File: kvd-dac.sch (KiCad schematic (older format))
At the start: 76 parts, among them J1 CONN_01X03, U1 ADG1412, U10 74HC595, U11 OPA2189, U12 MUX507, U13 AD8428, U14 AD8428, U15 AD8428, U16 AD8428, U17 OPA2189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

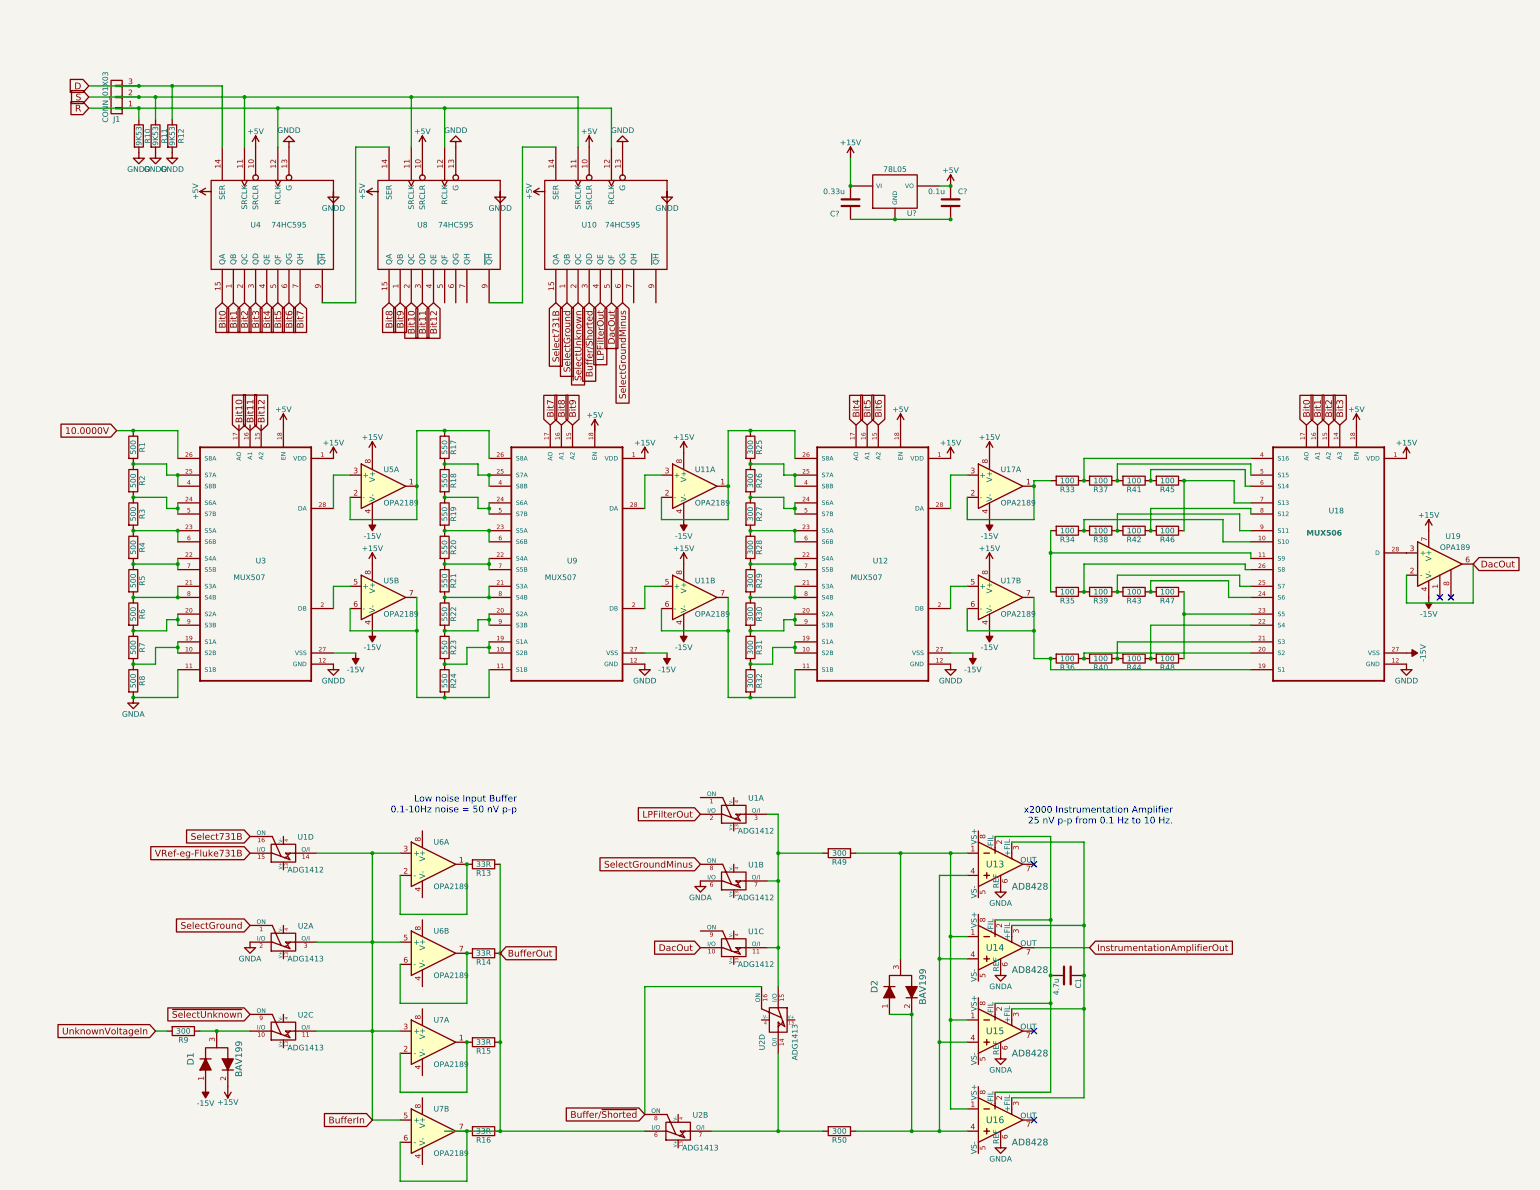
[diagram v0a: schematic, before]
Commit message: Add files via upload
Updated opamps to ada4522 because they have lower bias current.
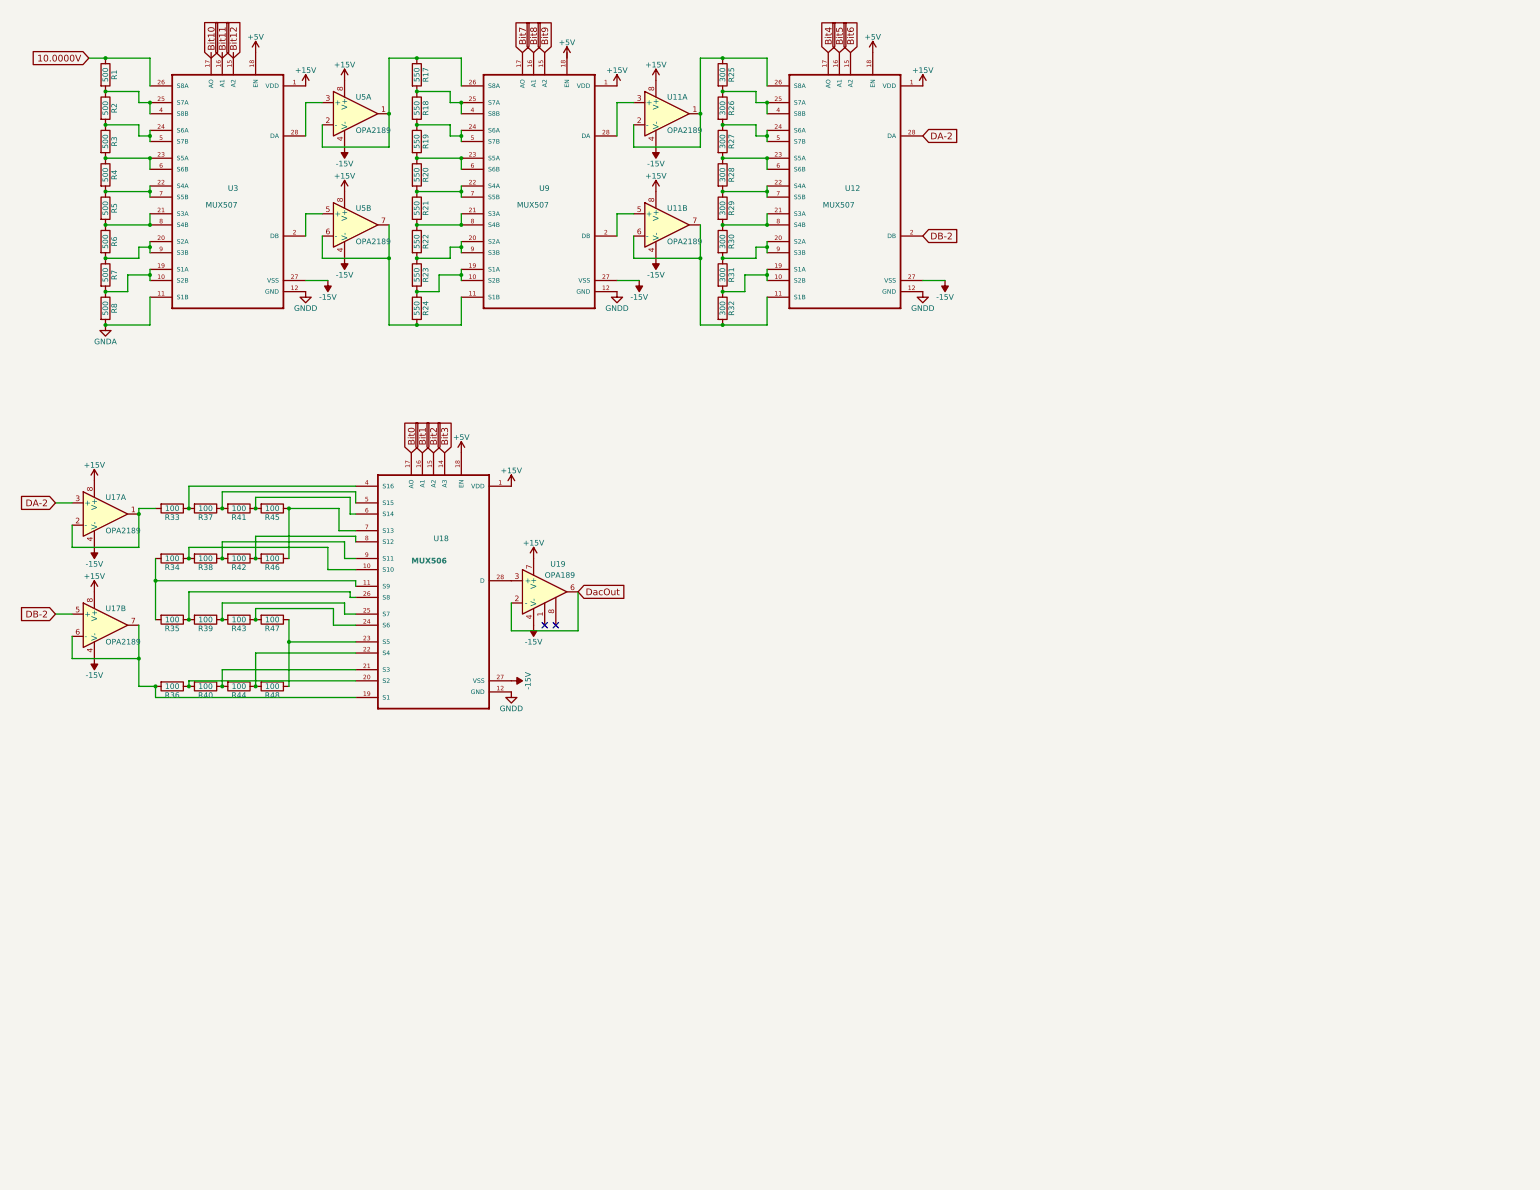
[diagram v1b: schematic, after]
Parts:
- removed C1: 4.7u, symbol C
- removed C?: 0.33u, symbol C
- removed C?: 0.1u, symbol C
- removed D1, D2: BAV199, digikey-footprints:SOT-23-3, symbol BAV99_LTB
- removed J1: CONN_01X03, symbol CONN_01X03
- removed R10, R11, R12: 9K53, symbol R
- removed R13, R14, R15, R16: 33R, symbol R
- removed R49, R50, R9: 300, symbol R
- removed U1: ADG1412, symbol DG308
- removed U10, U4, U8: 74HC595, symbol 74HC595
- removed U13, U14, U15, U16: AD8428, symbol AD8428
- removed U2: ADG1413, symbol DG308
- removed U6, U7: OPA2189, symbol TLC272
- removed U?: 78L05, symbol 78L05
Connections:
- net DB-2: now reaches U12.2 (DB), U17.5 (+)
- net DA-2: now reaches U12.28 (DA), U17.3 (+)
- net GND renamed GNDD
- no-connect marks 5 -> 2
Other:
- note removed: "Low noise Input Buffer\n0.1-10Hz noise = 50 nV p-p"
- note removed: "x2000 Instrumentation Amplifier\n25 nV p-p from 0.1 Hz to 10 Hz."
- moved on the sheet: R1, R17, R18, R19, R2, R20, R21, R22, R23, R24, R25, R26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
